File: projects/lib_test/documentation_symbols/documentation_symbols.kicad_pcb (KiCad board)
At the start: 2 copper layers, 100 x 100 mm, 1 part

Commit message: updated test projects
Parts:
- moved DOC1001 3.00 mm to (107.0, 55.0)
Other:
- board size 100 x 100 mm -> 40 x 20 mm
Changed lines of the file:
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@@
 (kicad_pcb
-	(version 20240108)
+	(version 20241229)
 	(generator "pcbnew")
-	(generator_version "8.0")
+	(generator_version "9.0")
 	(general
 		(thickness 1.6)
@@
 	(title_block
 		(title "Documentation symbols")
-		(date "2025-02-08")
+		(date "2025-05-24")
 		(rev "1")
 		(comment 1 "-")
@@
 	(layers
 		(0 "F.Cu" signal)
-		(31 "B.Cu" signal)
-		(34 "B.Paste" user)
-		(35 "F.Paste" user)
-		(36 "B.SilkS" user "B.Silkscreen")
-		(37 "F.SilkS" user "F.Silkscreen")
-		(38 "B.Mask" user)
-		(39 "F.Mask" user)
-		(40 "Dwgs.User" user "User.Drawings")
-		(41 "Cmts.User" user "User.Comments")
-		(44 "Edge.Cuts" user)
-		(45 "Margin" user)
-		(46 "B.CrtYd" user "B.Courtyard")
-		(47 "F.CrtYd" user "F.Courtyard")
-		(48 "B.Fab" user)
-		(49 "F.Fab" user)
+		(2 "B.Cu" signal)
+		(13 "F.Paste" user)
+		(15 "B.Paste" user)
+		(5 "F.SilkS" user "F.Silkscreen")
+		(7 "B.SilkS" user "B.Silkscreen")
+		(1 "F.Mask" user)
+		(3 "B.Mask" user)
+		(17 "Dwgs.User" user "User.Drawings")
+		(19 "Cmts.User" user "User.Comments")
+		(25 "Edge.Cuts" user)
+		(27 "Margin" user)
+		(31 "F.CrtYd" user "F.Courtyard")
+		(29 "B.CrtYd" user "B.Courtyard")
+		(35 "F.Fab" user)
+		(33 "B.Fab" user)
 	)
 	(setup
@@
 		(pad_to_mask_clearance 0)
 		(allow_soldermask_bridges_in_footprints no)
+		(tenting front back)
 		(pcbplotparams
-			(layerselection 0x00010fc_ffffffff)
-			(plot_on_all_layers_selection 0x0000000_00000000)
+			(layerselection 0x00000000_00000000_55555555_5755f5ff)
+			(plot_on_all_layers_selection 0x00000000_00000000_00000000_00000000)
 			(disableapertmacros no)
 			(usegerberextensions no)
@@
 			(svgprecision 6)
 			(plotframeref no)
-			(viasonmask no)
 			(mode 1)
 			(useauxorigin no)
@@
 			(pdf_front_fp_property_popups yes)
 			(pdf_back_fp_property_popups yes)
+			(pdf_metadata yes)
+			(pdf_single_document no)
 			(dxfpolygonmode yes)
 			(dxfimperialunits yes)
@@
 			(psnegative no)
 			(psa4output no)
-			(plotreference yes)
-			(plotvalue yes)
-			(plotfptext yes)
-			(plotinvisibletext no)
+			(plot_black_and_white yes)
 			(sketchpadsonfab no)
+			(plotpadnumbers no)
+			(hidednponfab no)
+			(sketchdnponfab yes)
+			(crossoutdnponfab yes)
 			(subtractmaskfromsilk no)
 			(outputformat 1)
@@
 	(footprint "lily_footprints:logo_lilytronics"
 		(layer "F.Cu")
-		(at 110 55)
+		(at 107 55)
 		(property "Reference" "DOC1001"
 			(at 0 -0.000002 0)
@@
 			)
 		)
-		(property "Footprint" "lily_footprints:logo_lilytronics"
+		(property "Datasheet" ""
 			(at 0 0 0)
 			(unlocked yes)
@@
 			)
 		)
-		(property "Datasheet" ""
+		(property "Description" ""
 			(at 0 0 0)
 			(unlocked yes)
@@
 			)
 		)
-		(property "Description" ""
-			(at 0 0 0)
-			(unlocked yes)
-			(layer "F.Fab")
-			(hide yes)
-			(effects
-				(font
-					(size 1.27 1.27)
-					(thickness 0.15)
-				)
-			)
-		)
 		(property "Revision" "1"
 			(at 0 0 0)
@@
 			)
 		)
-		(sheetname "Root")
+		(sheetname "/")
 		(sheetfile "documentation_symbols.kicad_sch")
 		(attr exclude_from_pos_files exclude_from_bom allow_missing_courtyard)
@@
 			)
 		)
-		(fp_text user "${REFERENCE}"
-			(at 0.000001 -0.000001 0)
-			(layer "F.Fab")
-			(hide yes)
-			(effects
-				(font
-					(size 0.5 0.5)
-					(thickness 0.1)
-				)
-			)
-		)
+		(embedded_fonts no)
 	)
 	(gr_rect
 		(start 100 50)
-		(end 200 150)
+		(end 140 70)
 		(stroke
 			(width 0.1)
 			(type default)
 		)
-		(fill none)
+		(fill no)
 		(layer "Edge.Cuts")
 	)
+	(embedded_fonts no)
 )

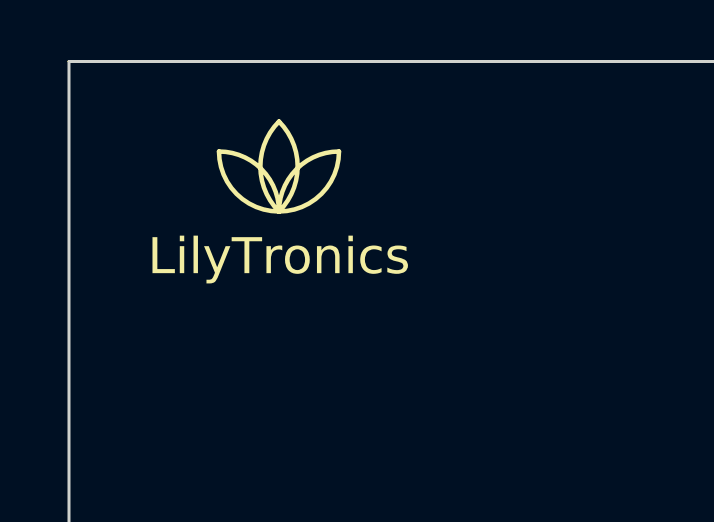
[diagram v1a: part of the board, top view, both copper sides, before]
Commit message: updated documentation test design
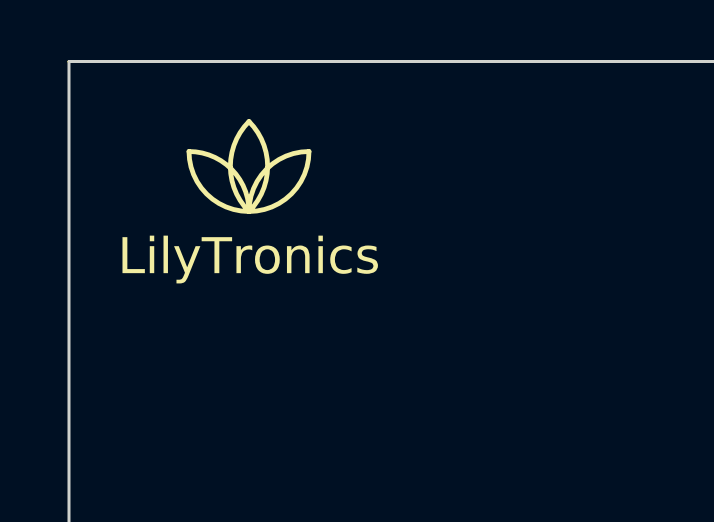
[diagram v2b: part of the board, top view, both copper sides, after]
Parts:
- DOC1001: value logo_lilytronics -> doc_logo_lilytronics; footprint lily_footprints:logo_lilytronics -> lily_footprints:doc_logo_lilytronics
- moved DOC1001 1.00 mm to (106.0, 55.0)
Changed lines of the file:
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@@
 	)
 	(net 0 "")
-	(footprint "lily_footprints:logo_lilytronics"
+	(footprint "lily_footprints:doc_logo_lilytronics"
 		(layer "F.Cu")
-		(at 107 55)
+		(at 106 55)
 		(property "Reference" "DOC1001"
 			(at 0 -0.000002 0)
@@
 			(effects
 				(font
-					(size 1 1)
-					(thickness 0.15)
+					(size 0.8 0.8)
+					(thickness 0.16)
 				)
 			)
 		)
-		(property "Value" "logo_lilytronics"
+		(property "Value" "doc_logo_lilytronics"
 			(at 0 0 0)
 			(layer "F.Fab")
@@
 			(end 0.000001 -0.000001)
 			(stroke
-				(width 0.15)
+				(width 0.16)
 				(type solid)
 			)
@@
 		(fp_arc
 			(start 0 0)
-			(mid 0.585786 -1.414214)
+			(mid 0.585786 -1.414213)
 			(end 2 -2)
 			(stroke
-				(width 0.15)
+				(width 0.16)
 				(type solid)
 			)
@@
 			(end 0.000001 -0.000001)
 			(stroke
-				(width 0.15)
+				(width 0.16)
 				(type solid)
 			)
@@
 			(end 0.000001 -2.999999)
 			(stroke
-				(width 0.15)
+				(width 0.16)
 				(type solid)
 			)
@@
 			(end -2 -2)
 			(stroke
-				(width 0.15)
+				(width 0.16)
 				(type solid)
 			)
